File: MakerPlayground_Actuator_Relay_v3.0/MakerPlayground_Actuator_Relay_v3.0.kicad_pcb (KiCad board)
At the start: 2 copper layers, 45.5 x 32 mm, 11 parts, among them J1 Conn_01x04, J2 Terminal Block, J3 Terminal Block, K1 SANYOU_SRD_Form_C, Q1 Q_NPN_BEC

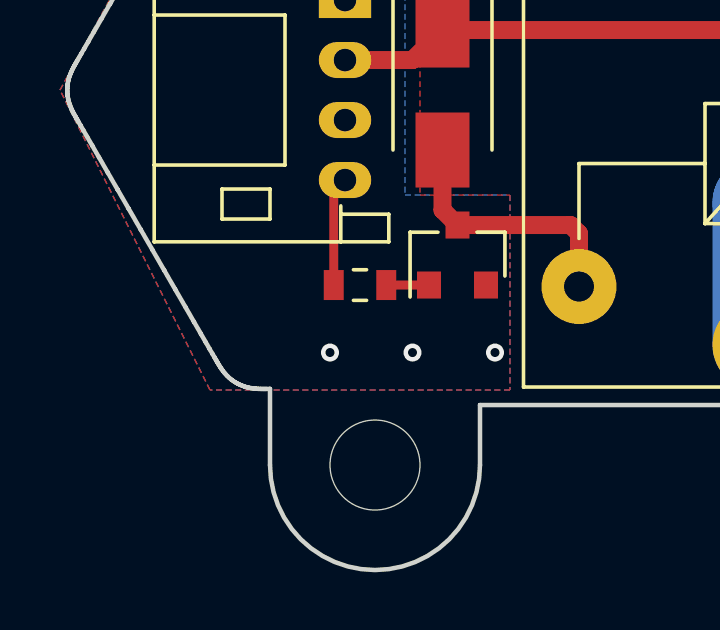
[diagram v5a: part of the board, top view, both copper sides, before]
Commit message: Fix missing MP 2x2 logo.
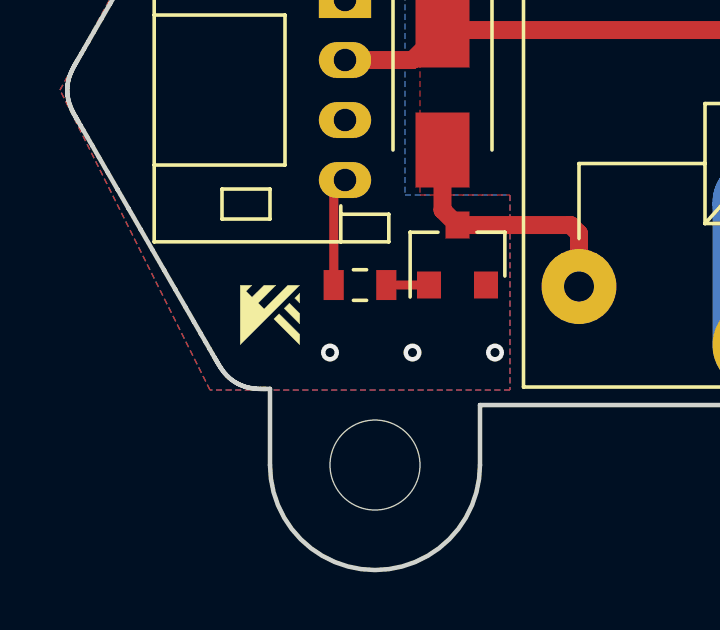
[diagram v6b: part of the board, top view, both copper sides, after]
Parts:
- added G***: LOGO, GiraffeTech-Utility:MakerPlayground_logo_2x2mm, F.Cu at (127.5, 107.5)
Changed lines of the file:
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@@
     (tracks 26)
     (zones 0)
-    (modules 11)
+    (modules 12)
     (nets 11)
   )
   (page A4)
   (layers
-    (0 F.Cu signal hide)
-    (31 B.Cu signal hide)
+    (0 F.Cu signal)
+    (31 B.Cu signal)
     (32 B.Adhes user)
     (33 F.Adhes user)
@@
     (39 F.Mask user hide)
     (40 Dwgs.User user)
-    (41 Cmts.User user)
-    (42 Eco1.User user)
-    (43 Eco2.User user)
+    (41 Cmts.User user hide)
+    (42 Eco1.User user hide)
+    (43 Eco2.User user hide)
     (44 Edge.Cuts user)
-    (45 Margin user)
-    (46 B.CrtYd user)
-    (47 F.CrtYd user)
+    (45 Margin user hide)
+    (46 B.CrtYd user hide)
+    (47 F.CrtYd user hide)
     (48 B.Fab user hide)
     (49 F.Fab user hide)
   )
   (setup
-    (last_trace_width 2.5)
+    (last_trace_width 0.25)
     (user_trace_width 0.25)
     (user_trace_width 0.3)
@@
     (pad 1 np_thru_hole circle (at 0 0) (size 3 3) (drill 3) (layers *.Cu *.Mask))
   )
+  (module GiraffeTech-Utility:MakerPlayground_logo_2x2mm (layer F.Cu)
+    (at 127.5 107.5)
+    (fp_text reference G*** (at 0 0) (layer F.SilkS) hide
+      (effects (font (size 1.524 1.524) (thickness 0.3)))
+    )
+    (fp_text value LOGO (at 0.75 0) (layer F.SilkS) hide
+      (effects (font (size 1.524 1.524) (thickness 0.3)))
+    )
+    (fp_poly (pts (xy 0.992188 -0.564543) (xy 0.992164 -0.528929) (xy 0.992097 -0.495895) (xy 0.991991 -0.466261)
+      (xy 0.991852 -0.440843) (xy 0.991684 -0.420459) (xy 0.991492 -0.405926) (xy 0.991282 -0.398062)
+      (xy 0.99116 -0.396875) (xy 0.988207 -0.399571) (xy 0.980351 -0.407199) (xy 0.968291 -0.419067)
+      (xy 0.952725 -0.434484) (xy 0.934354 -0.452758) (xy 0.913876 -0.4732) (xy 0.906847 -0.480231)
+      (xy 0.823563 -0.563586) (xy 0.907875 -0.647899) (xy 0.992188 -0.732211) (xy 0.992188 -0.564543)) (layer F.SilkS) (width 0.01))
+    (fp_poly (pts (xy 0.992272 -0.049513) (xy 0.991238 0.124084) (xy 0.990203 0.297682) (xy 0.731231 0.038685)
+      (xy 0.472259 -0.220311) (xy 0.559597 -0.307581) (xy 0.646934 -0.394851) (xy 0.992272 -0.049513)) (layer F.SilkS) (width 0.01))
+    (fp_poly (pts (xy 0.306845 -0.036934) (xy 0.315366 -0.028902) (xy 0.328804 -0.015931) (xy 0.346812 0.001638)
+      (xy 0.369045 0.023463) (xy 0.39516 0.049204) (xy 0.424812 0.078521) (xy 0.457655 0.111071)
+      (xy 0.493344 0.146515) (xy 0.531535 0.184511) (xy 0.571883 0.224719) (xy 0.614044 0.266798)
+      (xy 0.649934 0.302669) (xy 0.992273 0.645025) (xy 0.990203 0.990203) (xy 0.559594 0.560703)
+      (xy 0.128984 0.131202) (xy 0.214278 0.045757) (xy 0.235683 0.024442) (xy 0.255382 0.005068)
+      (xy 0.272657 -0.011676) (xy 0.28679 -0.025103) (xy 0.297063 -0.034528) (xy 0.302757 -0.039261)
+      (xy 0.303583 -0.039687) (xy 0.306845 -0.036934)) (layer F.SilkS) (width 0.01))
+    (fp_poly (pts (xy 0.790777 -0.991434) (xy 0.988227 -0.990203) (xy -0.992187 0.990197) (xy -0.992187 -0.992187)
+      (xy -0.601395 -0.992187) (xy -0.646963 -0.945555) (xy -0.665935 -0.926151) (xy -0.688266 -0.903332)
+      (xy -0.711752 -0.879346) (xy -0.734194 -0.856442) (xy -0.745114 -0.845303) (xy -0.797697 -0.791685)
+      (xy -0.698482 -0.692529) (xy -0.599266 -0.593373) (xy -0.399829 -0.79278) (xy -0.200393 -0.992187)
+      (xy 0.195473 -0.992187) (xy -0.099139 -0.695955) (xy -0.39375 -0.399723) (xy -0.194618 -0.200591)
+      (xy 0.199355 -0.596628) (xy 0.593328 -0.992663) (xy 0.790777 -0.991434)) (layer F.SilkS) (width 0.01))
+  )
   (gr_line (start 158.25 100.25) (end 158.75 99.75) (layer F.SilkS) (width 0.2))
